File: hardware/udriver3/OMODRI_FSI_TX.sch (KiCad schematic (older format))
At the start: 9 parts, among them J8 Conn_01x08, U16 TPD6E05U06, U17 DSLVDS1047PWR

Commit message: All footprints are present. DRV with 2 power branches.
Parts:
- removed C140: 100nF, Capacitor_SMD:C_0201_0603Metric, symbol Device:C
- removed J8: Conn_01x08, symbol Connector_Generic:Conn_01x08
- removed R85: 10k, Resistor_SMD:R_0201_0603Metric, symbol Device:R
- added J13: Conn_01x07, Connector_Hirose:Hirose_DF13-07P-1.25DSA_1x07_P1.25mm_Vertical, symbol Connector_Generic:Conn_01x07
- U15: renamed from U16; DigiKey (none) -> 296-39349-1-ND; Mouser (none) -> 595-TPD6E05U06RVZR; Part No (none) -> TPD6E05U06RVZR
- U16: renamed from U17; value DSLVDS1047PWR -> DSLVDS1047; DigiKey (none) -> 296-50740-1-ND; Mouser (none) -> 595-DSLVDS1047PWR; Part No (none) -> DSLVDS1047PWR
- renumbered C141 to C147, R82 to R77, R83 to R78, R84 to R79
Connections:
- net labels removed: TX_FSI_EN
- wire segments 54 -> 47
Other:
- moved on the sheet: R77, R78, R79

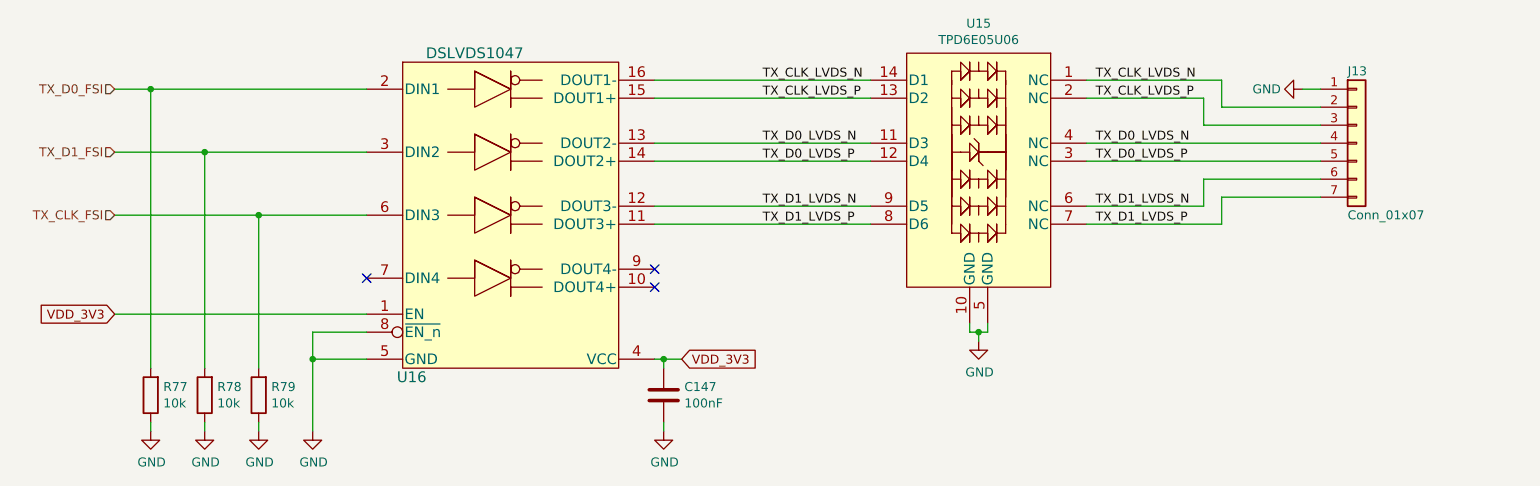
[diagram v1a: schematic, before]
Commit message: First complete release. No EtherCAT, IO ready to be connected.
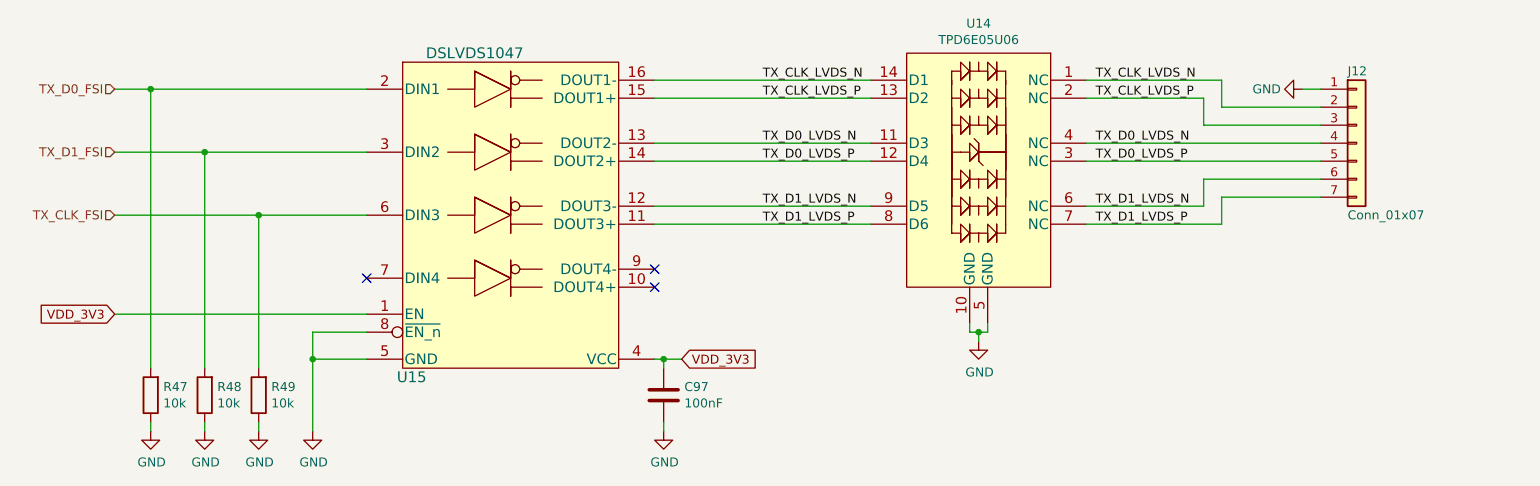
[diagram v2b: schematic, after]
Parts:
- renumbered C147 to C97, J13 to J12, R77 to R47, R78 to R48, R79 to R49, U15 to U14, U16 to U15
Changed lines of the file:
@@
 $Descr A4 11693 8268
 encoding utf-8
-Sheet 10 10
+Sheet 8 10
 Title "Open MOtor DRiver Initiative (OMODRI)"
 Date ""
@@
 AR Path="/5F7A5BAE/5F7AC1D4" Ref="U?"  Part="1"
 AR Path="/5F68F8CB/5F7AC1D4" Ref="U?"  Part="1"
-AR Path="/5F4C38EC/5F7AC1D4" Ref="U16"  Part="1"
-F 0 "U16" H 3800 2550 60  0000 C CNN
+AR Path="/5F4C38EC/5F7AC1D4" Ref="U?"  Part="1"
+AR Path="/5F5DA2EB/5F7AC1D4" Ref="U15"  Part="1"
+F 0 "U15" H 3800 2550 60  0000 C CNN
 F 1 "DSLVDS1047" H 4150 4350 60  0000 C CNN
 F 2 "Package_SO:TSSOP-16_4.4x5mm_P0.65mm" H 4000 2550 60  0001 C CNN
@@
 AR Path="/5F7A5BAE/5F569485" Ref="#PWR?"  Part="1"
 AR Path="/5F68F8CB/5F569485" Ref="#PWR?"  Part="1"
-AR Path="/5F4C38EC/5F569485" Ref="#PWR0147"  Part="1"
-F 0 "#PWR0147" H 5200 4500 50  0001 C CNN
+AR Path="/5F4C38EC/5F569485" Ref="#PWR?"  Part="1"
+AR Path="/5F5DA2EB/5F569485" Ref="#PWR0118"  Part="1"
+F 0 "#PWR0118" H 5200 4500 50  0001 C CNN
 F 1 "GND" H 5205 4577 50  0000 C CNN
 F 2 "" H 5200 4750 50  0001 C CNN
@@
 AR Path="/5F7A5BAE/5F569491" Ref="C?"  Part="1"
 AR Path="/5F68F8CB/5F569491" Ref="C?"  Part="1"
-AR Path="/5F4C38EC/5F569491" Ref="C147"  Part="1"
-F 0 "C147" H 5315 4596 50  0000 L CNN
+AR Path="/5F4C38EC/5F569491" Ref="C?"  Part="1"
+AR Path="/5F5DA2EB/5F569491" Ref="C97"  Part="1"
+F 0 "C97" H 5315 4596 50  0000 L CNN
 F 1 "100nF" H 5315 4505 50  0000 L CNN
 F 2 "Capacitor_SMD:C_0201_0603Metric" H 5238 4400 50  0001 C CNN
@@
 AR Path="/5F7A5BAE/5F56D312" Ref="#PWR?"  Part="1"
 AR Path="/5F68F8CB/5F56D312" Ref="#PWR?"  Part="1"
-AR Path="/5F4C38EC/5F56D312" Ref="#PWR0146"  Part="1"
-F 0 "#PWR0146" H 3250 4500 50  0001 C CNN
+AR Path="/5F4C38EC/5F56D312" Ref="#PWR?"  Part="1"
+AR Path="/5F5DA2EB/5F56D312" Ref="#PWR0117"  Part="1"
+F 0 "#PWR0117" H 3250 4500 50  0001 C CNN
 F 1 "GND" H 3255 4577 50  0000 C CNN
 F 2 "" H 3250 4750 50  0001 C CNN
@@
 AR Path="/5F7A5BAE/5F577EDA" Ref="R?"  Part="1"
 AR Path="/5F68F8CB/5F577EDA" Ref="R?"  Part="1"
-AR Path="/5F4C38EC/5F577EDA" Ref="R77"  Part="1"
-F 0 "R77" H 2280 4504 50  0000 R CNN
+AR Path="/5F4C38EC/5F577EDA" Ref="R?"  Part="1"
+AR Path="/5F5DA2EB/5F577EDA" Ref="R47"  Part="1"
+F 0 "R47" H 2280 4504 50  0000 R CNN
 F 1 "10k" H 2280 4595 50  0000 R CNN
 F 2 "Resistor_SMD:R_0201_0603Metric" V 2280 4550 50  0001 C CNN
@@
 AR Path="/5F7A5BAE/5F581FFF" Ref="R?"  Part="1"
 AR Path="/5F68F8CB/5F581FFF" Ref="R?"  Part="1"
-AR Path="/5F4C38EC/5F581FFF" Ref="R78"  Part="1"
-F 0 "R78" H 2580 4504 50  0000 R CNN
+AR Path="/5F4C38EC/5F581FFF" Ref="R?"  Part="1"
+AR Path="/5F5DA2EB/5F581FFF" Ref="R48"  Part="1"
+F 0 "R48" H 2580 4504 50  0000 R CNN
 F 1 "10k" H 2580 4595 50  0000 R CNN
 F 2 "Resistor_SMD:R_0201_0603Metric" V 2580 4550 50  0001 C CNN
@@
 AR Path="/5F7A5BAE/5F582480" Ref="R?"  Part="1"
 AR Path="/5F68F8CB/5F582480" Ref="R?"  Part="1"
-AR Path="/5F4C38EC/5F582480" Ref="R79"  Part="1"
-F 0 "R79" H 2880 4504 50  0000 R CNN
+AR Path="/5F4C38EC/5F582480" Ref="R?"  Part="1"
+AR Path="/5F5DA2EB/5F582480" Ref="R49"  Part="1"
+F 0 "R49" H 2880 4504 50  0000 R CNN
 F 1 "10k" H 2880 4595 50  0000 R CNN
 F 2 "Resistor_SMD:R_0201_0603Metric" V 2880 4550 50  0001 C CNN
@@
 AR Path="/5F7A5BAE/5F5828A2" Ref="#PWR?"  Part="1"
 AR Path="/5F68F8CB/5F5828A2" Ref="#PWR?"  Part="1"
-AR Path="/5F4C38EC/5F5828A2" Ref="#PWR0143"  Part="1"
-F 0 "#PWR0143" H 2350 4500 50  0001 C CNN
+AR Path="/5F4C38EC/5F5828A2" Ref="#PWR?"  Part="1"
+AR Path="/5F5DA2EB/5F5828A2" Ref="#PWR0114"  Part="1"
+F 0 "#PWR0114" H 2350 4500 50  0001 C CNN
 F 1 "GND" H 2355 4577 50  0000 C CNN
 F 2 "" H 2350 4750 50  0001 C CNN
@@
 AR Path="/5F7A5BAE/5F582BB4" Ref="#PWR?"  Part="1"
 AR Path="/5F68F8CB/5F582BB4" Ref="#PWR?"  Part="1"
-AR Path="/5F4C38EC/5F582BB4" Ref="#PWR0144"  Part="1"
-F 0 "#PWR0144" H 2650 4500 50  0001 C CNN
+AR Path="/5F4C38EC/5F582BB4" Ref="#PWR?"  Part="1"
+AR Path="/5F5DA2EB/5F582BB4" Ref="#PWR0115"  Part="1"
+F 0 "#PWR0115" H 2650 4500 50  0001 C CNN
 F 1 "GND" H 2655 4577 50  0000 C CNN
 F 2 "" H 2650 4750 50  0001 C CNN
@@
 AR Path="/5F7A5BAE/5F582DED" Ref="#PWR?"  Part="1"
 AR Path="/5F68F8CB/5F582DED" Ref="#PWR?"  Part="1"
-AR Path="/5F4C38EC/5F582DED" Ref="#PWR0145"  Part="1"
-F 0 "#PWR0145" H 2950 4500 50  0001 C CNN
+AR Path="/5F4C38EC/5F582DED" Ref="#PWR?"  Part="1"
+AR Path="/5F5DA2EB/5F582DED" Ref="#PWR0116"  Part="1"
+F 0 "#PWR0116" H 2950 4500 50  0001 C CNN
 F 1 "GND" H 2955 4577 50  0000 C CNN
 F 2 "" H 2950 4750 50  0001 C CNN
@@
 AR Path="/5F7A5BAE/5F5F778E" Ref="U?"  Part="1"
 AR Path="/5F68F8CB/5F5F778E" Ref="U?"  Part="1"
-AR Path="/5F4C38EC/5F5F778E" Ref="U15"  Part="1"
-F 0 "U15" H 6950 3915 50  0000 C CNN
+AR Path="/5F4C38EC/5F5F778E" Ref="U?"  Part="1"
+AR Path="/5F5DA2EB/5F5F778E" Ref="U14"  Part="1"
+F 0 "U14" H 6950 3915 50  0000 C CNN
 F 1 "TPD6E05U06" H 6950 3824 50  0000 C CNN
 F 2 "udrive3:USON_14" V 6950 3200 50  0001 C CNN
@@
 AR Path="/5F7A5BAE/5F60EB6A" Ref="#PWR?"  Part="1"
 AR Path="/5F68F8CB/5F60EB6A" Ref="#PWR?"  Part="1"
-AR Path="/5F4C38EC/5F60EB6A" Ref="#PWR0142"  Part="1"
-F 0 "#PWR0142" H 6950 4000 50  0001 C CNN
+AR Path="/5F4C38EC/5F60EB6A" Ref="#PWR?"  Part="1"
+AR Path="/5F5DA2EB/5F60EB6A" Ref="#PWR0113"  Part="1"
+F 0 "#PWR0113" H 6950 4000 50  0001 C CNN
 F 1 "GND" H 6955 4077 50  0000 C CNN
 F 2 "" H 6950 4250 50  0001 C CNN
@@
 	7550 3250 8850 3250
 $Comp
-L Connector_Generic:Conn_01x07 J13
+L Connector_Generic:Conn_01x07 J?
 U 1 1 5F6FBF4B
 P 9050 3150
-F 0 "J13" H 9000 3550 50  0000 L CNN
+AR Path="/5F4C38EC/5F6FBF4B" Ref="J?"  Part="1"
+AR Path="/5F5DA2EB/5F6FBF4B" Ref="J12"  Part="1"
+F 0 "J12" H 9000 3550 50  0000 L CNN
 F 1 "Conn_01x07" H 9000 2750 50  0000 L CNN
 F 2 "Connector_Hirose:Hirose_DF13-07P-1.25DSA_1x07_P1.25mm_Vertical" H 9050 3150 50  0001 C CNN
@@
 AR Path="/5F7A5BAE/5F6FD413" Ref="#PWR?"  Part="1"
 AR Path="/5F68F8CB/5F6FD413" Ref="#PWR?"  Part="1"
-AR Path="/5F4C38EC/5F6FD413" Ref="#PWR0141"  Part="1"
-F 0 "#PWR0141" H 8750 2600 50  0001 C CNN
+AR Path="/5F4C38EC/5F6FD413" Ref="#PWR?"  Part="1"
+AR Path="/5F5DA2EB/5F6FD413" Ref="#PWR0112"  Part="1"
+F 0 "#PWR0112" H 8750 2600 50  0001 C CNN
 F 1 "GND" V 8750 2650 50  0000 C CNN
 F 2 "" H 8750 2850 50  0001 C CNN

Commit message: Update of the schematics. Driver and power files split. Placement starting.
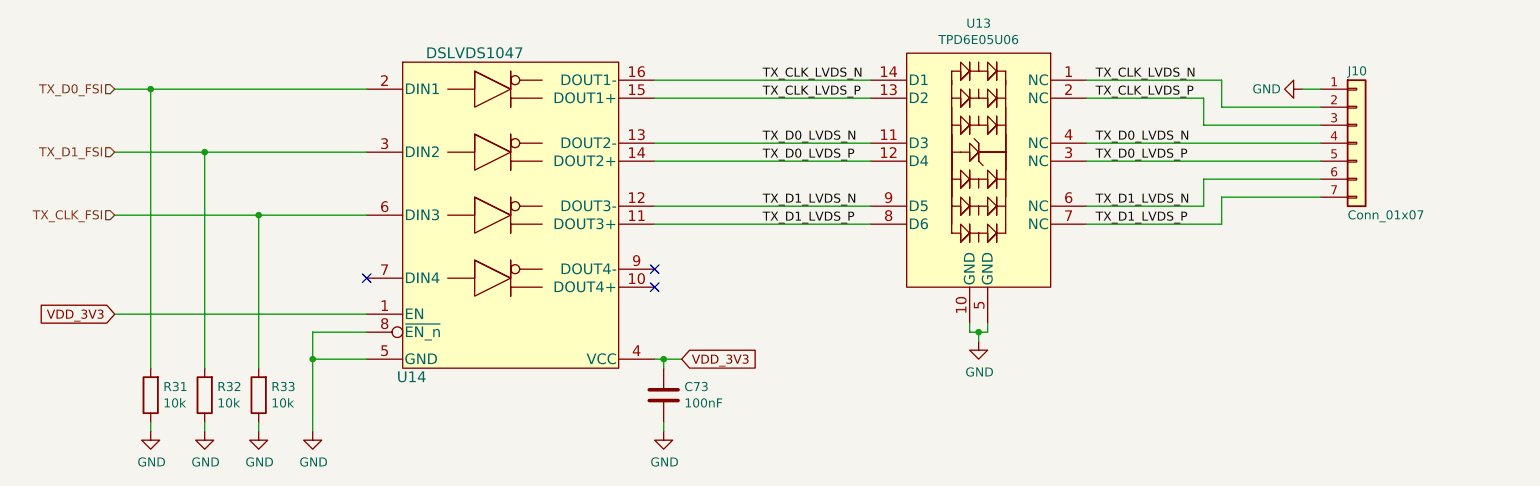
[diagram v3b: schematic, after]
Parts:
- J10: renamed from J12; DigiKey (none) -> DF13-7P-1.25DSA(75)-ND; Mouser (none) -> 798-DF13-7P-125DSA75; Part No (none) -> DF13-7P-1.25DSA(75); RS (none) -> 188-6250
- U13: renamed from U14; footprint udrive3:USON_14 -> udriver3:USON_14
- renumbered C97 to C73, R47 to R31, R48 to R32, R49 to R33, U15 to U14
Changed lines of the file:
@@
 $Descr A4 11693 8268
 encoding utf-8
-Sheet 8 10
+Sheet 7 17
 Title "Open MOtor DRiver Initiative (OMODRI)"
 Date ""
@@
 AR Path="/5F68F8CB/5F7AC1D4" Ref="U?"  Part="1"
 AR Path="/5F4C38EC/5F7AC1D4" Ref="U?"  Part="1"
-AR Path="/5F5DA2EB/5F7AC1D4" Ref="U15"  Part="1"
-F 0 "U15" H 3800 2550 60  0000 C CNN
+AR Path="/5F5DA2EB/5F7AC1D4" Ref="U14"  Part="1"
+F 0 "U14" H 3800 2550 60  0000 C CNN
 F 1 "DSLVDS1047" H 4150 4350 60  0000 C CNN
 F 2 "Package_SO:TSSOP-16_4.4x5mm_P0.65mm" H 4000 2550 60  0001 C CNN
@@
 AR Path="/5F68F8CB/5F569485" Ref="#PWR?"  Part="1"
 AR Path="/5F4C38EC/5F569485" Ref="#PWR?"  Part="1"
-AR Path="/5F5DA2EB/5F569485" Ref="#PWR0118"  Part="1"
-F 0 "#PWR0118" H 5200 4500 50  0001 C CNN
+AR Path="/5F5DA2EB/5F569485" Ref="#PWR093"  Part="1"
+F 0 "#PWR093" H 5200 4500 50  0001 C CNN
 F 1 "GND" H 5205 4577 50  0000 C CNN
 F 2 "" H 5200 4750 50  0001 C CNN
@@
 AR Path="/5F68F8CB/5F569491" Ref="C?"  Part="1"
 AR Path="/5F4C38EC/5F569491" Ref="C?"  Part="1"
-AR Path="/5F5DA2EB/5F569491" Ref="C97"  Part="1"
-F 0 "C97" H 5315 4596 50  0000 L CNN
+AR Path="/5F5DA2EB/5F569491" Ref="C73"  Part="1"
+F 0 "C73" H 5315 4596 50  0000 L CNN
 F 1 "100nF" H 5315 4505 50  0000 L CNN
 F 2 "Capacitor_SMD:C_0201_0603Metric" H 5238 4400 50  0001 C CNN
@@
 AR Path="/5F68F8CB/5F56D312" Ref="#PWR?"  Part="1"
 AR Path="/5F4C38EC/5F56D312" Ref="#PWR?"  Part="1"
-AR Path="/5F5DA2EB/5F56D312" Ref="#PWR0117"  Part="1"
-F 0 "#PWR0117" H 3250 4500 50  0001 C CNN
+AR Path="/5F5DA2EB/5F56D312" Ref="#PWR092"  Part="1"
+F 0 "#PWR092" H 3250 4500 50  0001 C CNN
 F 1 "GND" H 3255 4577 50  0000 C CNN
 F 2 "" H 3250 4750 50  0001 C CNN
@@
 AR Path="/5F68F8CB/5F577EDA" Ref="R?"  Part="1"
 AR Path="/5F4C38EC/5F577EDA" Ref="R?"  Part="1"
-AR Path="/5F5DA2EB/5F577EDA" Ref="R47"  Part="1"
-F 0 "R47" H 2280 4504 50  0000 R CNN
+AR Path="/5F5DA2EB/5F577EDA" Ref="R31"  Part="1"
+F 0 "R31" H 2280 4504 50  0000 R CNN
 F 1 "10k" H 2280 4595 50  0000 R CNN
 F 2 "Resistor_SMD:R_0201_0603Metric" V 2280 4550 50  0001 C CNN
@@
 AR Path="/5F68F8CB/5F581FFF" Ref="R?"  Part="1"
 AR Path="/5F4C38EC/5F581FFF" Ref="R?"  Part="1"
-AR Path="/5F5DA2EB/5F581FFF" Ref="R48"  Part="1"
-F 0 "R48" H 2580 4504 50  0000 R CNN
+AR Path="/5F5DA2EB/5F581FFF" Ref="R32"  Part="1"
+F 0 "R32" H 2580 4504 50  0000 R CNN
 F 1 "10k" H 2580 4595 50  0000 R CNN
 F 2 "Resistor_SMD:R_0201_0603Metric" V 2580 4550 50  0001 C CNN
@@
 AR Path="/5F68F8CB/5F582480" Ref="R?"  Part="1"
 AR Path="/5F4C38EC/5F582480" Ref="R?"  Part="1"
-AR Path="/5F5DA2EB/5F582480" Ref="R49"  Part="1"
-F 0 "R49" H 2880 4504 50  0000 R CNN
+AR Path="/5F5DA2EB/5F582480" Ref="R33"  Part="1"
+F 0 "R33" H 2880 4504 50  0000 R CNN
 F 1 "10k" H 2880 4595 50  0000 R CNN
 F 2 "Resistor_SMD:R_0201_0603Metric" V 2880 4550 50  0001 C CNN
@@
 AR Path="/5F68F8CB/5F5828A2" Ref="#PWR?"  Part="1"
 AR Path="/5F4C38EC/5F5828A2" Ref="#PWR?"  Part="1"
-AR Path="/5F5DA2EB/5F5828A2" Ref="#PWR0114"  Part="1"
-F 0 "#PWR0114" H 2350 4500 50  0001 C CNN
+AR Path="/5F5DA2EB/5F5828A2" Ref="#PWR089"  Part="1"
+F 0 "#PWR089" H 2350 4500 50  0001 C CNN
 F 1 "GND" H 2355 4577 50  0000 C CNN
 F 2 "" H 2350 4750 50  0001 C CNN
@@
 AR Path="/5F68F8CB/5F582BB4" Ref="#PWR?"  Part="1"
 AR Path="/5F4C38EC/5F582BB4" Ref="#PWR?"  Part="1"
-AR Path="/5F5DA2EB/5F582BB4" Ref="#PWR0115"  Part="1"
-F 0 "#PWR0115" H 2650 4500 50  0001 C CNN
+AR Path="/5F5DA2EB/5F582BB4" Ref="#PWR090"  Part="1"
+F 0 "#PWR090" H 2650 4500 50  0001 C CNN
 F 1 "GND" H 2655 4577 50  0000 C CNN
 F 2 "" H 2650 4750 50  0001 C CNN
@@
 AR Path="/5F68F8CB/5F582DED" Ref="#PWR?"  Part="1"
 AR Path="/5F4C38EC/5F582DED" Ref="#PWR?"  Part="1"
-AR Path="/5F5DA2EB/5F582DED" Ref="#PWR0116"  Part="1"
-F 0 "#PWR0116" H 2950 4500 50  0001 C CNN
+AR Path="/5F5DA2EB/5F582DED" Ref="#PWR091"  Part="1"
+F 0 "#PWR091" H 2950 4500 50  0001 C CNN
 F 1 "GND" H 2955 4577 50  0000 C CNN
 F 2 "" H 2950 4750 50  0001 C CNN
@@
 AR Path="/5F68F8CB/5F5F778E" Ref="U?"  Part="1"
 AR Path="/5F4C38EC/5F5F778E" Ref="U?"  Part="1"
-AR Path="/5F5DA2EB/5F5F778E" Ref="U14"  Part="1"
-F 0 "U14" H 6950 3915 50  0000 C CNN
+AR Path="/5F5DA2EB/5F5F778E" Ref="U13"  Part="1"
+F 0 "U13" H 6950 3915 50  0000 C CNN
 F 1 "TPD6E05U06" H 6950 3824 50  0000 C CNN
-F 2 "udrive3:USON_14" V 6950 3200 50  0001 C CNN
+F 2 "udriver3:USON_14" V 6950 3200 50  0001 C CNN
 F 3 "https://www.ti.com/lit/ds/symlink/tpd6e05u06.pdf" V 6950 3200 50  0001 C CNN
 F 4 "296-39349-1-ND" H 6950 3200 50  0001 C CNN "DigiKey"
@@
 AR Path="/5F68F8CB/5F60EB6A" Ref="#PWR?"  Part="1"
 AR Path="/5F4C38EC/5F60EB6A" Ref="#PWR?"  Part="1"
-AR Path="/5F5DA2EB/5F60EB6A" Ref="#PWR0113"  Part="1"
-F 0 "#PWR0113" H 6950 4000 50  0001 C CNN
+AR Path="/5F5DA2EB/5F60EB6A" Ref="#PWR088"  Part="1"
+F 0 "#PWR088" H 6950 4000 50  0001 C CNN
 F 1 "GND" H 6955 4077 50  0000 C CNN
 F 2 "" H 6950 4250 50  0001 C CNN
@@
 P 9050 3150
 AR Path="/5F4C38EC/5F6FBF4B" Ref="J?"  Part="1"
-AR Path="/5F5DA2EB/5F6FBF4B" Ref="J12"  Part="1"
-F 0 "J12" H 9000 3550 50  0000 L CNN
+AR Path="/5F5DA2EB/5F6FBF4B" Ref="J10"  Part="1"
+F 0 "J10" H 9000 3550 50  0000 L CNN
 F 1 "Conn_01x07" H 9000 2750 50  0000 L CNN
 F 2 "Connector_Hirose:Hirose_DF13-07P-1.25DSA_1x07_P1.25mm_Vertical" H 9050 3150 50  0001 C CNN
-F 3 "~" H 9050 3150 50  0001 C CNN
+F 3 "https://www.hirose.com/product/document?clcode=&productname=&series=DF13&documenttype=Catalog&lang=en&documentid=D31687_en" H 9050 3150 50  0001 C CNN
+F 4 "DF13-7P-1.25DSA(75)-ND" H 9050 3150 50  0001 C CNN "DigiKey"
+F 5 "798-DF13-7P-125DSA75" H 9050 3150 50  0001 C CNN "Mouser"
+F 6 "DF13-7P-1.25DSA(75)" H 9050 3150 50  0001 C CNN "Part No"
+F 7 "188-6250" H 9050 3150 50  0001 C CNN "RS"
 	1    9050 3150
 	1    0    0    -1
@@
 AR Path="/5F68F8CB/5F6FD413" Ref="#PWR?"  Part="1"
 AR Path="/5F4C38EC/5F6FD413" Ref="#PWR?"  Part="1"
-AR Path="/5F5DA2EB/5F6FD413" Ref="#PWR0112"  Part="1"
-F 0 "#PWR0112" H 8750 2600 50  0001 C CNN
+AR Path="/5F5DA2EB/5F6FD413" Ref="#PWR087"  Part="1"
+F 0 "#PWR087" H 8750 2600 50  0001 C CNN
 F 1 "GND" V 8750 2650 50  0000 C CNN
 F 2 "" H 8750 2850 50  0001 C CNN

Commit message: Update of the schematics. Switches on GPIO72 & GPIO84 are missing. J1, J2 & J14 must be merged and connector placement optimized. TCXO must be changed from 20MHz to 25MHz for EtherCAT compatibility. PCB is partially routed in 6-Layers (mainly power supplies and and transistors). 8-Layers will be necessary.
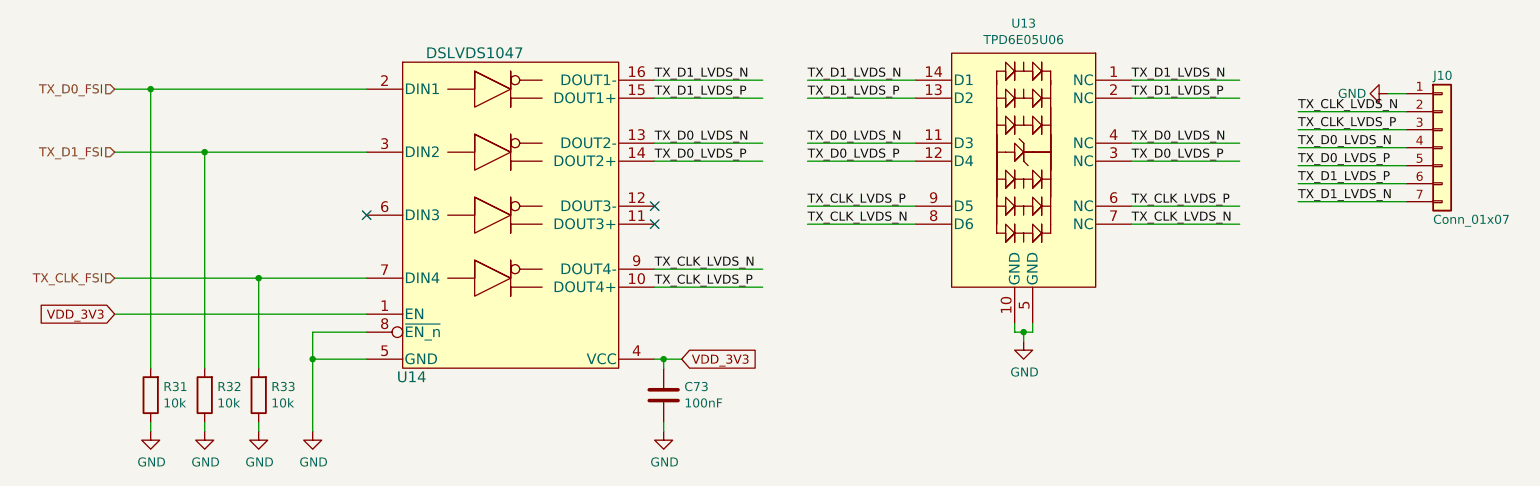
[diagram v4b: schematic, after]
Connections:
- wire segments 47 -> 51
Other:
- moved on the sheet: J10, U13

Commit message: First release of the fully routed OMODRI PCB from LAAS. (8 layers)
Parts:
- J10: footprint Connector_Hirose:Hirose_DF13-07P-1.25DSA_1x07_P1.25mm_Vertical -> udriver3:Hirose_DF13-07P-1.25DSA_1x07_P1.25mm_Vertical
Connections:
- net labels added: TX_FSI_CLK, TX_FSI_D0, TX_FSI_D1
- net labels removed: TX_CLK_FSI, TX_D0_FSI, TX_D1_FSI
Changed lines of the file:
@@
 $Descr A4 11693 8268
 encoding utf-8
-Sheet 11 17
+Sheet 9 19
 Title "Open MOtor DRiver Initiative (OMODRI)"
 Date ""
@@
 	1    0    0    -1
 $EndComp
-Text Label 6000 3600 0    50   ~ 0
+Text Label 6025 2800 0    50   ~ 0
 TX_CLK_LVDS_N
-Text Label 6000 3500 0    50   ~ 0
+Text Label 6025 2900 0    50   ~ 0
 TX_CLK_LVDS_P
-Text Label 6000 3250 0    50   ~ 0
+Text Label 6025 3150 0    50   ~ 0
 TX_D0_LVDS_P
-Text Label 6000 3150 0    50   ~ 0
+Text Label 6025 3250 0    50   ~ 0
 TX_D0_LVDS_N
-Text Label 6000 2900 0    50   ~ 0
+Text Label 6025 3500 0    50   ~ 0
 TX_D1_LVDS_P
-Text Label 6000 2800 0    50   ~ 0
+Text Label 6025 3600 0    50   ~ 0
 TX_D1_LVDS_N
 Text GLabel 5300 4350 2    50   Input ~ 0
@@
 $EndComp
 Text HLabel 2150 3900 0    50   Input ~ 0
-TX_CLK_FSI
+TX_FSI_CLK
 Text HLabel 2150 2850 0    50   Input ~ 0
-TX_D0_FSI
+TX_FSI_D0
 Text HLabel 2150 3200 0    50   Input ~ 0
-TX_D1_FSI
+TX_FSI_D1
 $Comp
 L Device:R R?
@@
 F 0 "J10" H 9475 3575 50  0000 L CNN
 F 1 "Conn_01x07" H 9475 2775 50  0000 L CNN
-F 2 "Connector_Hirose:Hirose_DF13-07P-1.25DSA_1x07_P1.25mm_Vertical" H 9525 3175 50  0001 C CNN
+F 2 "udriver3:Hirose_DF13-07P-1.25DSA_1x07_P1.25mm_Vertical" H 9525 3175 50  0001 C CNN
 F 3 "https://www.hirose.com/product/document?clcode=&productname=&series=DF13&documenttype=Catalog&lang=en&documentid=D31687_en" H 9525 3175 50  0001 C CNN
 F 4 "DF13-7P-1.25DSA(75)-ND" H 9525 3175 50  0001 C CNN "DigiKey"
@@
 Wire Wire Line
 	6000 2900 6600 2900
+Text Label 7800 2800 0    50   ~ 0
+TX_CLK_LVDS_N
+Text Label 7825 3150 0    50   ~ 0
+TX_D0_LVDS_P
+Text Label 7825 3250 0    50   ~ 0
+TX_D0_LVDS_N
+Text Label 7800 3500 0    50   ~ 0
+TX_D1_LVDS_P
 Text Label 7800 3600 0    50   ~ 0
-TX_CLK_LVDS_N
-Text Label 7800 3250 0    50   ~ 0
-TX_D0_LVDS_P
-Text Label 7800 3150 0    50   ~ 0
-TX_D0_LVDS_N
-Text Label 7800 2900 0    50   ~ 0
-TX_D1_LVDS_P
-Text Label 7800 2800 0    50   ~ 0
 TX_D1_LVDS_N
 Wire Wire Line
@@
 Wire Wire Line
 	2950 3900 3550 3900
-Text Label 7800 3500 0    50   ~ 0
+Text Label 7800 2900 0    50   ~ 0
 TX_CLK_LVDS_P
 NoConn ~ 3550 3550
